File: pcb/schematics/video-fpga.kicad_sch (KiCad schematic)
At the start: 42 parts, among them U4 LCMXO2-7000HC-4TG144C, X1 ASV-xxxMHz

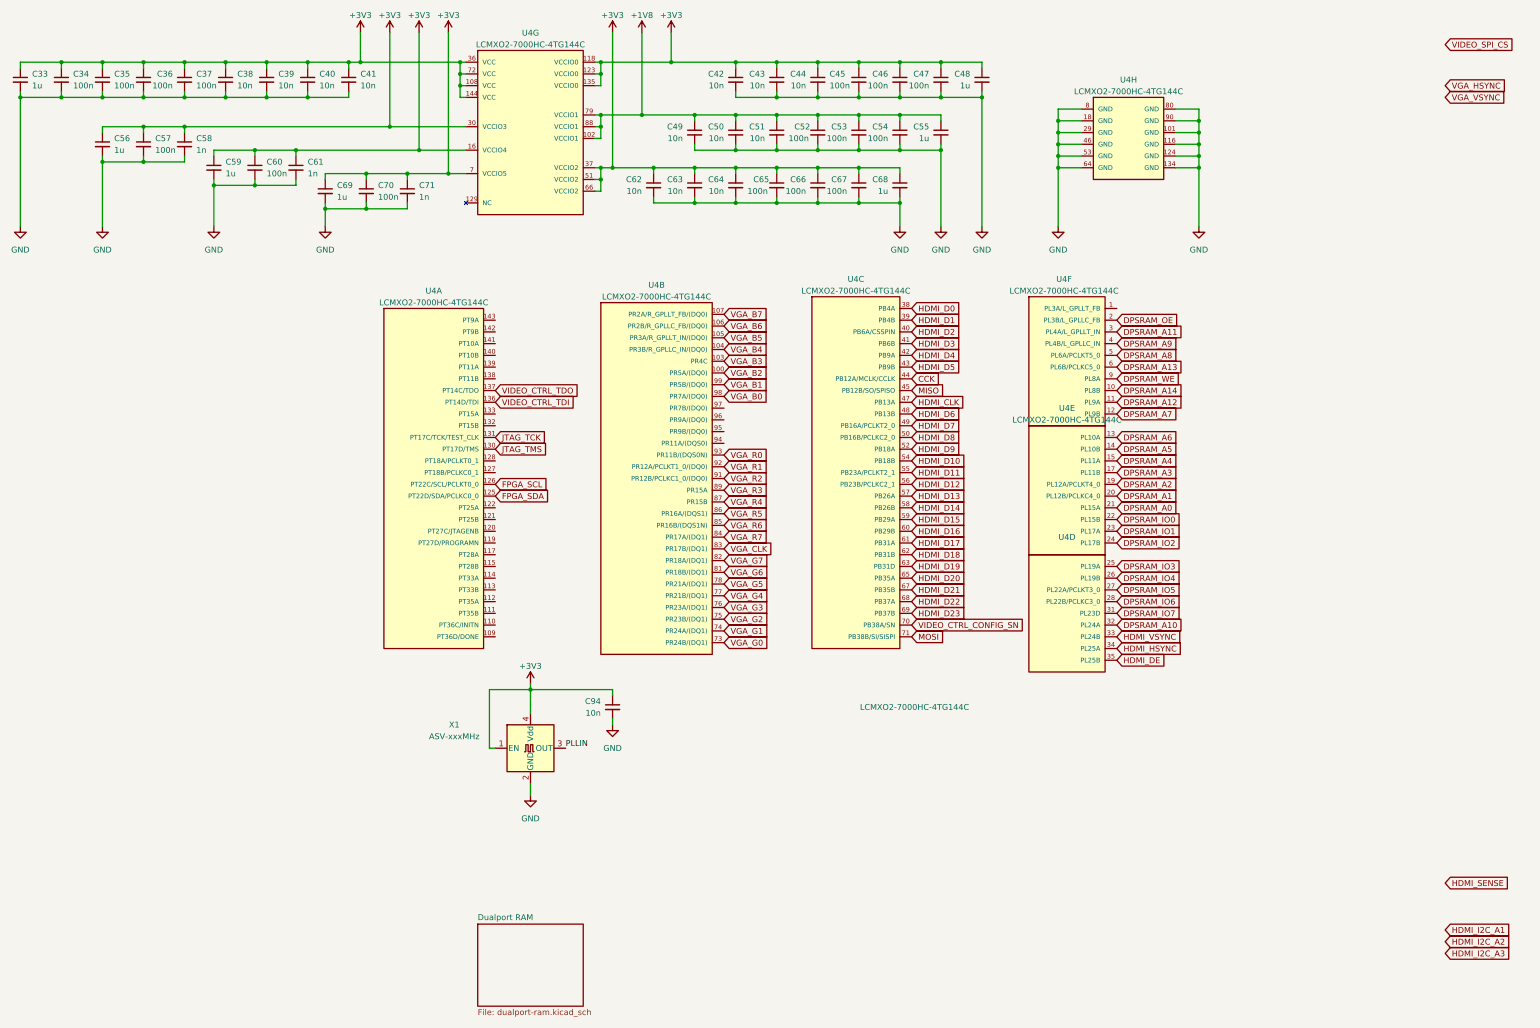
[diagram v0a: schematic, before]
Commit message: add the 3v3 voltage regulator
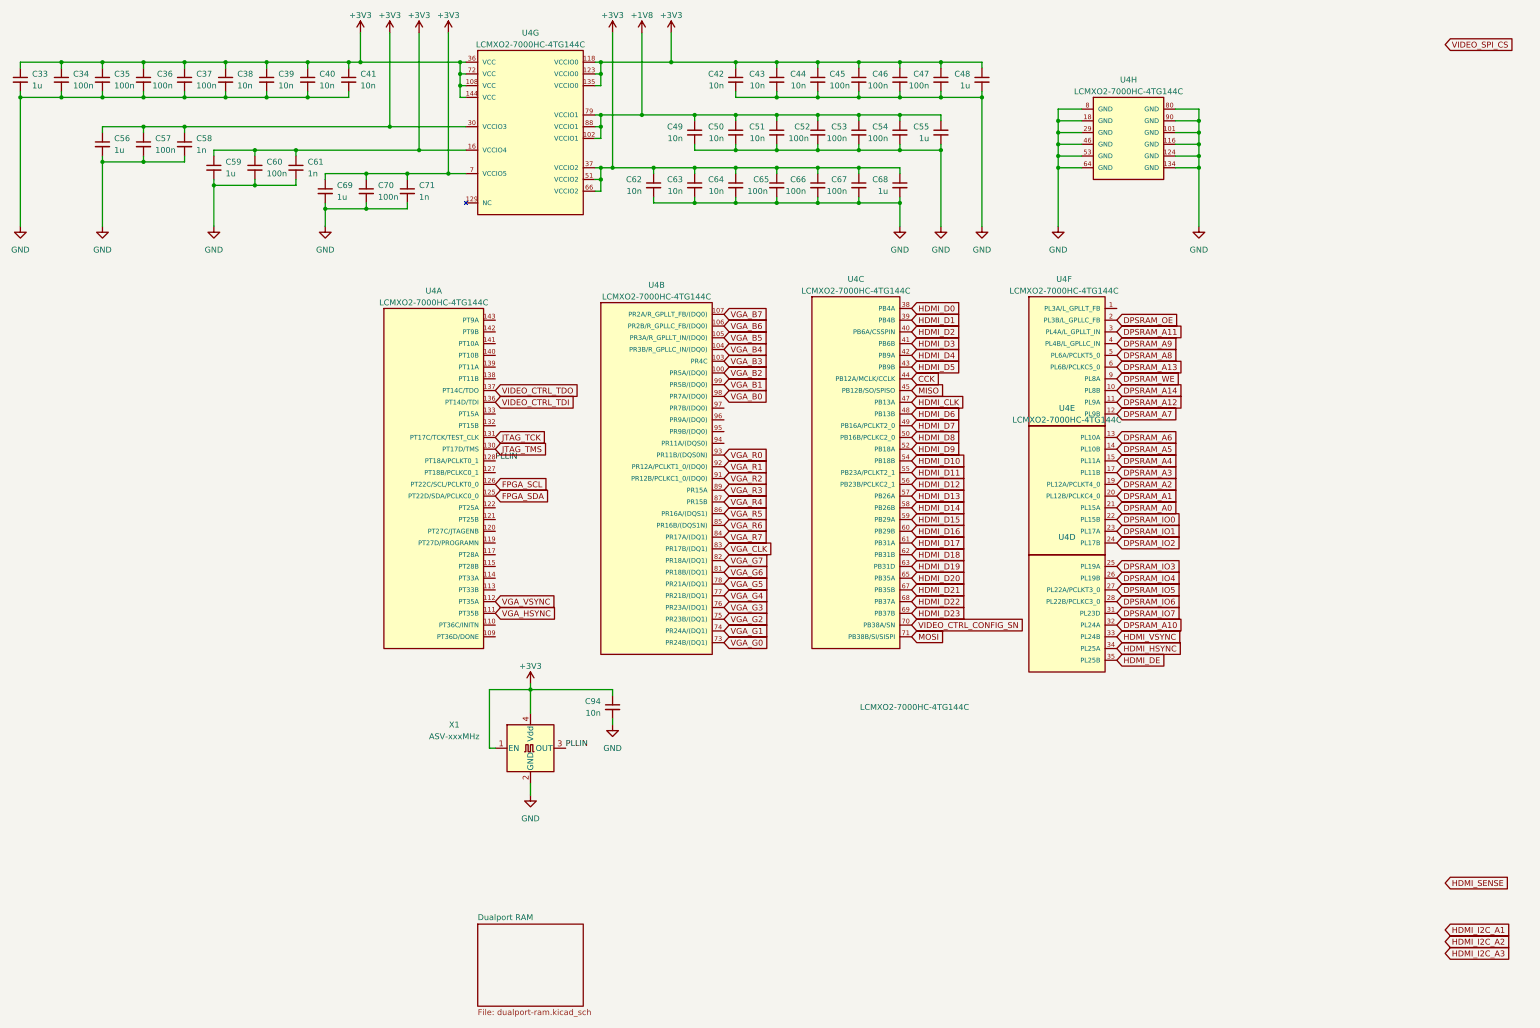
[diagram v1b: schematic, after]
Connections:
- net PLLIN: now also U4.128 (PT18A/PCLKT0_1)
- net VGA_HSYNC: now also U4.111 (PT35B)
- net VGA_VSYNC: now also U4.112 (PT35A)
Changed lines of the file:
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@@
     (effects (font (size 1.27 1.27)) (justify left bottom))
   )
+  (label "PLLIN" (at 119.38 114.3 0) (fields_autoplaced)
+    (effects (font (size 1.27 1.27)) (justify left bottom))
+  )
   (global_label "HDMI_D7" (shape input) (at 209.55 106.68 0)
     (effects (font (size 1.27 1.27)) (justify left))
@@
     )
   )
-  (global_label "VGA_HSYNC" (shape input) (at 325.12 33.02 0) (fields_autoplaced)
-    (effects (font (size 1.27 1.27)) (justify left))
-    (property "Intersheetrefs" "${INTERSHEET_REFS}" (id 0) (at 338.606 33.02 0)
+  (global_label "VGA_HSYNC" (shape input) (at 119.38 147.32 0) (fields_autoplaced)
+    (effects (font (size 1.27 1.27)) (justify left))
+    (property "Intersheetrefs" "${INTERSHEET_REFS}" (id 0) (at 132.866 147.32 0)
       (effects (font (size 1.27 1.27)) (justify left))
     )
@@
     )
   )
-  (global_label "VGA_VSYNC" (shape input) (at 325.12 35.56 0) (fields_autoplaced)
-    (effects (font (size 1.27 1.27)) (justify left))
-    (property "Intersheetrefs" "${INTERSHEET_REFS}" (id 0) (at 338.3641 35.56 0)
-      (effects (font (size 1.27 1.27)) (justify left))
-    )
+  (global_label "VGA_VSYNC" (shape input) (at 119.38 144.78 0) (fields_autoplaced)
+    (effects (font (size 1.27 1.27)) (justify left))
+    (property "Intersheetrefs" "${INTERSHEET_REFS}" (id 0) (at 132.6241 144.78 0)
+      (effects (font (size 1.27 1.27)) (justify left))
+    )

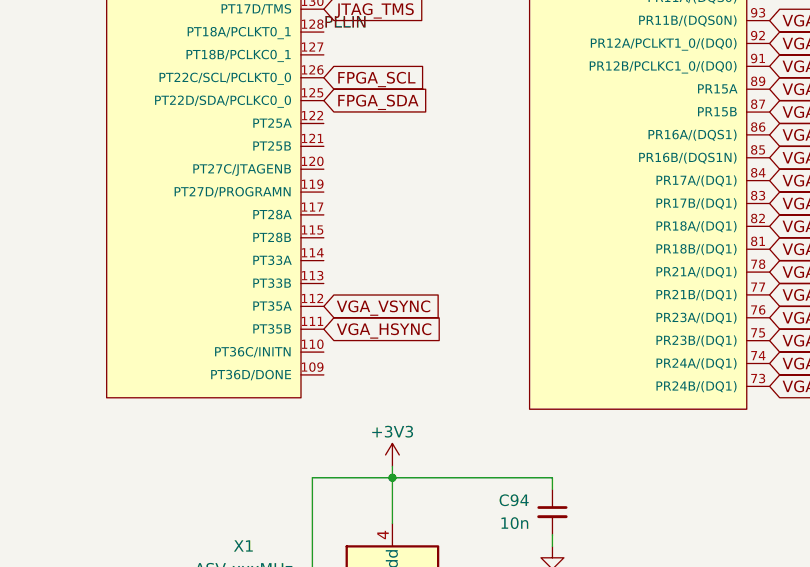
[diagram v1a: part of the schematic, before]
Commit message: add the programming controller
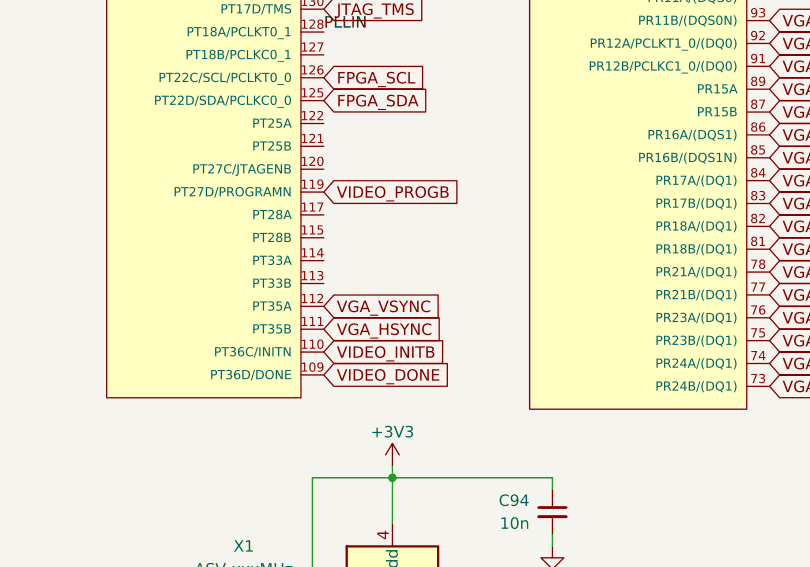
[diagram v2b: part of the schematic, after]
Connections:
- net VIDEO_DONE: now reaches U4.109 (PT36D/DONE)
- net VIDEO_INITB: now reaches U4.110 (PT36C/INITN)
- net VIDEO_PROGB: now reaches U4.119 (PT27D/PROGRAMN)
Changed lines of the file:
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@@
+    )
+  )
+  (global_label "VIDEO_INITB" (shape input) (at 119.38 149.86 0) (fields_autoplaced)
+    (effects (font (size 1.27 1.27)) (justify left))
+    (property "Intersheetrefs" "${INTERSHEET_REFS}" (id 0) (at 133.4103 149.86 0)
+      (effects (font (size 1.27 1.27)) (justify left))
     )
   )
@@
     )
   )
+  (global_label "VIDEO_PROGB" (shape input) (at 119.38 132.08 0) (fields_autoplaced)
+    (effects (font (size 1.27 1.27)) (justify left))
+    (property "Intersheetrefs" "${INTERSHEET_REFS}" (id 0) (at 135.0431 132.08 0)
+      (effects (font (size 1.27 1.27)) (justify left))
+    )
+  )
   (global_label "FPGA_SDA" (shape input) (at 119.38 121.92 0)
     (effects (font (size 1.27 1.27)) (justify left))
@@
       (effects (font (size 1.27 1.27)) (justify left))
     )
+  )
+  (global_label "VIDEO_DONE" (shape input) (at 119.38 152.4 0) (fields_autoplaced)
+    (effects (font (size 1.27 1.27)) (justify left))
+    (property "Intersheetrefs" "${INTERSHEET_REFS}" (id 0) (at 133.7126 152.4 0)
+      (effects (font (size 1.27 1.27)) (justify left))
+    )

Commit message: add shield
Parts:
- U: renamed from C67; value 100n -> (none); footprint Capacitor_SMD:C_0603_1608Metric -> (none)
- U: renamed from U4; value LCMXO2-7000HC-4TG144C -> (none); footprint LCMXO2-7000HC-4TG144C:Lattice_Semiconductor-LCMXO2-7000HC-4TG144C-Level_C -> (none)
- U: renamed from C64; value 10n -> (none); footprint Capacitor_SMD:C_0402_1005Metric -> (none)
- U: renamed from C52; value 100n -> (none); footprint Capacitor_SMD:C_0603_1608Metric -> (none)
- U: renamed from C57; value 100n -> (none); footprint Capacitor_SMD:C_0603_1608Metric -> (none)
- U: renamed from C66; value 100n -> (none); footprint Capacitor_SMD:C_0603_1608Metric -> (none)
- U: renamed from C63; value 10n -> (none); footprint Capacitor_SMD:C_0402_1005Metric -> (none)
- U: renamed from C33; value 1u -> (none); footprint Capacitor_SMD:C_0805_2012Metric -> (none)
- U: renamed from C42; value 10n -> (none); footprint Capacitor_SMD:C_0402_1005Metric -> (none)
- U: renamed from C43; value 10n -> (none); footprint Capacitor_SMD:C_0402_1005Metric -> (none)
- U: renamed from C37; value 100n -> (none); footprint Capacitor_SMD:C_0603_1608Metric -> (none)
- U: renamed from C55; value 1u -> (none); footprint Capacitor_SMD:C_0805_2012Metric -> (none)
- U: renamed from C71; value 1n -> (none); footprint Capacitor_SMD:C_0402_1005Metric -> (none)
- U: renamed from C41; value 10n -> (none); footprint Capacitor_SMD:C_0402_1005Metric -> (none)
- U: renamed from C48; value 1u -> (none); footprint Capacitor_SMD:C_0805_2012Metric -> (none)
- U: renamed from C61; value 1n -> (none); footprint Capacitor_SMD:C_0402_1005Metric -> (none)
- U: renamed from C35; value 100n -> (none); footprint Capacitor_SMD:C_0603_1608Metric -> (none)
- U: renamed from C56; value 1u -> (none); footprint Capacitor_SMD:C_0805_2012Metric -> (none)
- U: renamed from C34; value 100n -> (none); footprint Capacitor_SMD:C_0603_1608Metric -> (none)
- U: renamed from C53; value 100n -> (none); footprint Capacitor_SMD:C_0603_1608Metric -> (none)
- U: renamed from C51; value 10n -> (none); footprint Capacitor_SMD:C_0402_1005Metric -> (none)
- U: renamed from C58; value 1n -> (none); footprint Capacitor_SMD:C_0402_1005Metric -> (none)
- U: renamed from C44; value 10n -> (none); footprint Capacitor_SMD:C_0402_1005Metric -> (none)
- U: renamed from C49; value 10n -> (none); footprint Capacitor_SMD:C_0402_1005Metric -> (none)
- U: renamed from C60; value 100n -> (none); footprint Capacitor_SMD:C_0603_1608Metric -> (none)
- U: renamed from C39; value 10n -> (none); footprint Capacitor_SMD:C_0402_1005Metric -> (none)
- U: renamed from C36; value 100n -> (none); footprint Capacitor_SMD:C_0603_1608Metric -> (none)
- U: renamed from C50; value 10n -> (none); footprint Capacitor_SMD:C_0402_1005Metric -> (none)
- U: renamed from C69; value 1u -> (none); footprint Capacitor_SMD:C_0805_2012Metric -> (none)
- U: renamed from C54; value 100n -> (none); footprint Capacitor_SMD:C_0603_1608Metric -> (none)
- U: renamed from C59; value 1u -> (none); footprint Capacitor_SMD:C_0805_2012Metric -> (none)
- U: renamed from C45; value 100n -> (none); footprint Capacitor_SMD:C_0603_1608Metric -> (none)
- U: renamed from C70; value 100n -> (none); footprint Capacitor_SMD:C_0603_1608Metric -> (none)
- U: renamed from C38; value 10n -> (none); footprint Capacitor_SMD:C_0402_1005Metric -> (none)
- U: renamed from C94; value 10n -> (none); footprint Capacitor_SMD:C_0402_1005Metric -> (none)
- U: renamed from X1; value ASV-xxxMHz -> (none); footprint Oscillator:Oscillator_SMD_Abracon_ASV-4Pin_7.0x5.1mm -> (none)
- U: renamed from C40; value 10n -> (none); footprint Capacitor_SMD:C_0402_1005Metric -> (none)
- U: renamed from C65; value 100n -> (none); footprint Capacitor_SMD:C_0603_1608Metric -> (none)
- U: renamed from C68; value 1u -> (none); footprint Capacitor_SMD:C_0805_2012Metric -> (none)
- U: renamed from C46; value 100n -> (none); footprint Capacitor_SMD:C_0603_1608Metric -> (none)
- U: renamed from C62; value 10n -> (none); footprint Capacitor_SMD:C_0402_1005Metric -> (none)
- U: renamed from C47; value 100n -> (none); footprint Capacitor_SMD:C_0603_1608Metric -> (none)
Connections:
- net +1V8: no longer U.102 (VCCIO1), U.79 (VCCIO1), U.88 (VCCIO1)
- net +3V3: now also U.140 (PT10B), U.141 (PT10A), U.142 (PT9B), U.143 (PT9A); no longer U.108 (VCC), U.118 (VCCIO0), U.123 (VCCIO0), U.135 (VCCIO0), U.144 (VCC), U.16 (VCCIO4), U.30 (VCCIO3), U.36 (VCC), U.37 (VCCIO2), U.51 (VCCIO2), U.66 (VCCIO2), U.7 (VCCIO5), U.72 (VCC)
- net CCK: now also U.137 (PT14C/TDO); no longer U.44 (PB12A/MCLK/CCLK)
- net DPSRAM_A0: now also U.121 (PT25B), U.137 (PT14C/TDO); no longer U.21 (PL15A)
- net DPSRAM_A1: now also U.122 (PT25A), U.138 (PT11B); no longer U.20 (PL12B/PCLKC4_0)
- net DPSRAM_A10: now also U.109 (PT36D/DONE), U.122 (PT25A), U.138 (PT11B); no longer U.32 (PL24A)
- net DPSRAM_A11: now also U.141 (PT10A); no longer U.3 (PL4A/L_GPLLT_IN)
- net DPSRAM_A12: now also U.133 (PT15A); no longer U.11 (PL9A)
- net DPSRAM_A13: now also U.138 (PT11B); no longer U.6 (PL6B/PCLKC5_0)
- net DPSRAM_A14: now also U.136 (PT14D/TDI); no longer U.10 (PL8B)
- net DPSRAM_A2: now also U.125 (PT22D/SDA/PCLKC0_0), U.139 (PT11A); no longer U.19 (PL12A/PCLKT4_0)
- net DPSRAM_A3: now also U.126 (PT22C/SCL/PCLKT0_0), U.140 (PT10B); no longer U.17 (PL11B)
- net DPSRAM_A4: now also U.127 (PT18B/PCLKC0_1), U.141 (PT10A); no longer U.15 (PL11A)
- net DPSRAM_A5: now also U.128 (PT18A/PCLKT0_1), U.142 (PT9B); no longer U.14 (PL10B)
- net DPSRAM_A6: now also U.130 (PT17D/TMS), U.143 (PT9A); no longer U.13 (PL10A)
- net DPSRAM_A7: now also U.132 (PT15B); no longer U.12 (PL9B)
- net DPSRAM_A8: now also U.139 (PT11A); no longer U.5 (PL6A/PCLKT5_0)
- net DPSRAM_A9: now also U.140 (PT10B); no longer U.4 (PL4B/L_GPLLC_IN)
- net DPSRAM_IO0: now also U.120 (PT27C/JTAGENB), U.136 (PT14D/TDI); no longer U.22 (PL15B)
- net DPSRAM_IO1: now also U.119 (PT27D/PROGRAMN), U.133 (PT15A); no longer U.23 (PL17A)
- net DPSRAM_IO2: now also U.117 (PT28A), U.132 (PT15B); no longer U.24 (PL17B)
- net DPSRAM_IO3: now also U.114 (PT33A), U.130 (PT17D/TMS), U.143 (PT9A); no longer U.25 (PL19A)
- net DPSRAM_IO4: now also U.113 (PT33B), U.128 (PT18A/PCLKT0_1), U.142 (PT9B); no longer U.26 (PL19B)
- net DPSRAM_IO5: now also U.112 (PT35A), U.127 (PT18B/PCLKC0_1), U.141 (PT10A); no longer U.27 (PL22A/PCLKT3_0)
- net DPSRAM_IO6: now also U.111 (PT35B), U.126 (PT22C/SCL/PCLKT0_0), U.140 (PT10B); no longer U.28 (PL22B/PCLKC3_0)
- net DPSRAM_IO7: now also U.110 (PT36C/INITN), U.125 (PT22D/SDA/PCLKC0_0), U.139 (PT11A); no longer U.31 (PL23D)
- net DPSRAM_OE: now also U.142 (PT9B); no longer U.2 (PL3B/L_GPLLC_FB)
- net DPSRAM_WE: now also U.137 (PT14C/TDO); no longer U.9 (PL8A)
- net GND: now also U.138 (PT11B), U.139 (PT11A), U.140 (PT10B), U.141 (PT10A), U.142 (PT9B), U.143 (PT9A); no longer U.101 (GND), U.116 (GND), U.124 (GND), U.134 (GND), U.18 (GND), U.29 (GND), U.46 (GND), U.53 (GND), U.64 (GND), U.8 (GND), U.80 (GND), U.90 (GND)
- net HDMI_CLK: now also U.133 (PT15A); no longer U.47 (PB13A)
- net HDMI_D0: now also U.143 (PT9A); no longer U.38 (PB4A)
- net HDMI_D1: now also U.142 (PT9B); no longer U.39 (PB4B)
- net HDMI_D10: now also U.127 (PT18B/PCLKC0_1); no longer U.54 (PB18B)
- net HDMI_D11: now also U.126 (PT22C/SCL/PCLKT0_0); no longer U.55 (PB23A/PCLKT2_1)
- net HDMI_D12: now also U.125 (PT22D/SDA/PCLKC0_0); no longer U.56 (PB23B/PCLKC2_1)
- net HDMI_D13: now also U.122 (PT25A); no longer U.57 (PB26A)
- net HDMI_D14: now also U.121 (PT25B); no longer U.58 (PB26B)
- net HDMI_D15: now also U.120 (PT27C/JTAGENB); no longer U.59 (PB29A)
- net HDMI_D16: now also U.119 (PT27D/PROGRAMN); no longer U.60 (PB29B)
- net HDMI_D17: now also U.117 (PT28A); no longer U.61 (PB31A)
- net HDMI_D18: now also U.115 (PT28B); no longer U.62 (PB31B)
- net HDMI_D19: now also U.114 (PT33A); no longer U.63 (PB31D)
- net HDMI_D2: now also U.141 (PT10A); no longer U.40 (PB6A/CSSPIN)
- net HDMI_D20: now also U.113 (PT33B); no longer U.65 (PB35A)
- net HDMI_D21: now also U.112 (PT35A); no longer U.67 (PB35B)
- net HDMI_D22: now also U.111 (PT35B); no longer U.68 (PB37A)
- net HDMI_D23: now also U.110 (PT36C/INITN); no longer U.69 (PB37B)
- net HDMI_D3: now also U.140 (PT10B); no longer U.41 (PB6B)
- net HDMI_D4: now also U.139 (PT11A); no longer U.42 (PB9A)
- net HDMI_D5: now also U.138 (PT11B); no longer U.43 (PB9B)
- net HDMI_D6: now also U.132 (PT15B); no longer U.48 (PB13B)
- net HDMI_D7: now also U.131 (PT17C/TCK/TEST_CLK); no longer U.49 (PB16A/PCLKT2_0)
- net HDMI_D8: now also U.130 (PT17D/TMS); no longer U.50 (PB16B/PCLKC2_0)
- net HDMI_D9: now also U.128 (PT18A/PCLKT0_1); no longer U.52 (PB18A)
- net HDMI_DE: now also U.119 (PT27D/PROGRAMN), U.133 (PT15A); no longer U.35 (PL25B)
- net HDMI_HSYNC: now also U.120 (PT27C/JTAGENB), U.136 (PT14D/TDI); no longer U.34 (PL25A)
- net HDMI_VSYNC: now also U.121 (PT25B), U.137 (PT14C/TDO); no longer U.33 (PL24B)
- net MISO: now also U.136 (PT14D/TDI); no longer U.45 (PB12B/SO/SPISO)
- net MOSI: no longer U.71 (PB38B/SI/SISPI)
- net VGA_B0: now also U.136 (PT14D/TDI); no longer U.98 (PR7A/(DQ0))
- net VGA_B1: now also U.137 (PT14C/TDO); no longer U.99 (PR5B/(DQ0))
- net VGA_B2: now also U.138 (PT11B); no longer U.100 (PR5A/(DQ0))
- net VGA_B3: now also U.139 (PT11A); no longer U.103 (PR4C)
- net VGA_B4: now also U.140 (PT10B); no longer U.104 (PR3B/R_GPLLC_IN/(DQ0))
- net VGA_B5: now also U.141 (PT10A); no longer U.105 (PR3A/R_GPLLT_IN/(DQ0))
- net VGA_B6: now also U.142 (PT9B); no longer U.106 (PR2B/R_GPLLC_FB/(DQ0))
- net VGA_B7: now also U.143 (PT9A); no longer U.107 (PR2A/R_GPLLT_FB/(DQ0))
- net VGA_CLK: now also U.117 (PT28A); no longer U.83 (PR17B/(DQ1))
- net VGA_G0: no longer U.73 (PR24B/(DQ1))
- net VGA_G1: now also U.109 (PT36D/DONE); no longer U.74 (PR24A/(DQ1))
- net VGA_G2: now also U.110 (PT36C/INITN); no longer U.75 (PR23B/(DQ1))
- net VGA_G3: now also U.111 (PT35B); no longer U.76 (PR23A/(DQ1))
- net VGA_G4: now also U.112 (PT35A); no longer U.77 (PR21B/(DQ1))
- net VGA_G5: now also U.113 (PT33B); no longer U.78 (PR21A/(DQ1))
- net VGA_G6: now also U.114 (PT33A); no longer U.81 (PR18B/(DQ1))
- net VGA_G7: now also U.115 (PT28B); no longer U.82 (PR18A/(DQ1))
- net VGA_R0: now also U.128 (PT18A/PCLKT0_1); no longer U.93 (PR11B/(DQS0N))
- net VGA_R1: now also U.127 (PT18B/PCLKC0_1); no longer U.92 (PR12A/PCLKT1_0/(DQ0))
- net VGA_R2: now also U.126 (PT22C/SCL/PCLKT0_0); no longer U.91 (PR12B/PCLKC1_0/(DQ0))
- net VGA_R3: now also U.125 (PT22D/SDA/PCLKC0_0); no longer U.89 (PR15A)
- net VGA_R4: now also U.122 (PT25A); no longer U.87 (PR15B)
- net VGA_R5: now also U.121 (PT25B); no longer U.86 (PR16A/(DQS1))
- net VGA_R6: now also U.120 (PT27C/JTAGENB); no longer U.85 (PR16B/(DQS1N))
- net VGA_R7: now also U.119 (PT27D/PROGRAMN); no longer U.84 (PR17A/(DQ1))
- net VIDEO_CTRL_CONFIG_SN: now also U.109 (PT36D/DONE); no longer U.70 (PB38A/SN)
- new net: U.109 (PT36D/DONE), U.122 (PT25A)
- new net: U.110 (PT36C/INITN), U.125 (PT22D/SDA/PCLKC0_0)
- new net: U.111 (PT35B), U.126 (PT22C/SCL/PCLKT0_0)
- new net: U.112 (PT35A), U.127 (PT18B/PCLKC0_1)
- new net: U.113 (PT33B), U.128 (PT18A/PCLKT0_1)
- new net: U.114 (PT33A), U.130 (PT17D/TMS)
- new net: U.115 (PT28B), U.131 (PT17C/TCK/TEST_CLK) (x2)
- new net: U.117 (PT28A), U.132 (PT15B)

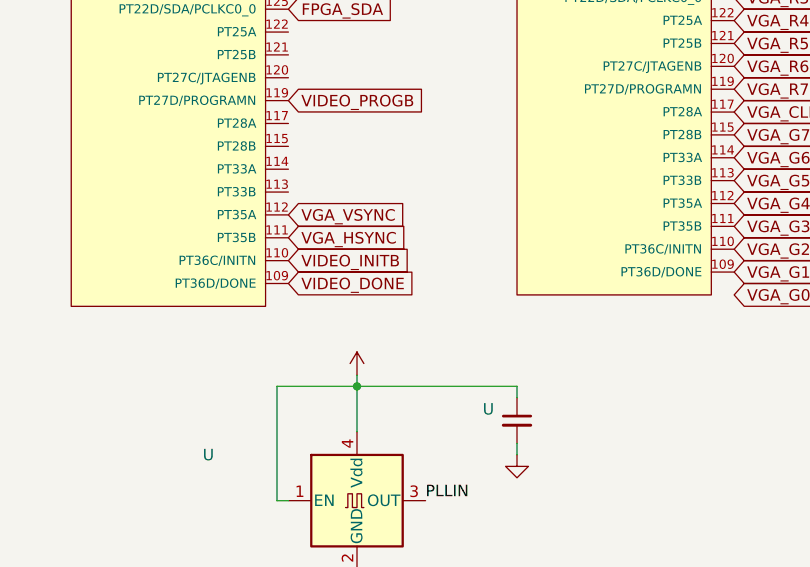
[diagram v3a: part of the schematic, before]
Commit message: add status led in the programming interface schematic
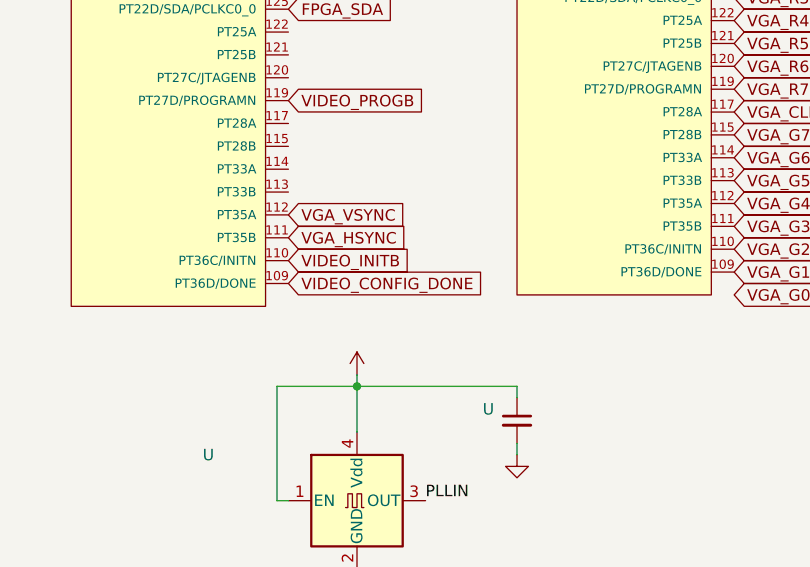
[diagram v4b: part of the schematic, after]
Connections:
- net VIDEO_DONE renamed VIDEO_CONFIG_DONE
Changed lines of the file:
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@@
     )
   )
-  (global_label "VIDEO_DONE" (shape input) (at 119.38 152.4 0) (fields_autoplaced)
+  (global_label "VIDEO_CONFIG_DONE" (shape input) (at 119.38 152.4 0) (fields_autoplaced)
     (effects (font (size 1.27 1.27)) (justify left))
-    (property "Intersheetrefs" "${INTERSHEET_REFS}" (id 0) (at 133.7126 152.4 0)
+    (property "Intersheetrefs" "${INTERSHEET_REFS}" (id 0) (at 141.5746 152.4 0)
       (effects (font (size 1.27 1.27)) (justify left))
     )
